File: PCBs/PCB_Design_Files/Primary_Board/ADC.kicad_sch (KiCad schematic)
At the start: 88 parts, among them U10 TMUX1133PWR, U11 MCP6561T-E/OT, U12 TMUX1133PWR, U13 LF398N/NOPB, U14 AD5621AKSZ, U15 TMUX1133PWR, U3 REF3333AIDBZR, U7 TMUX1104DGSR, U8 TMUX1133PWR, U9 TMUX1133PWR

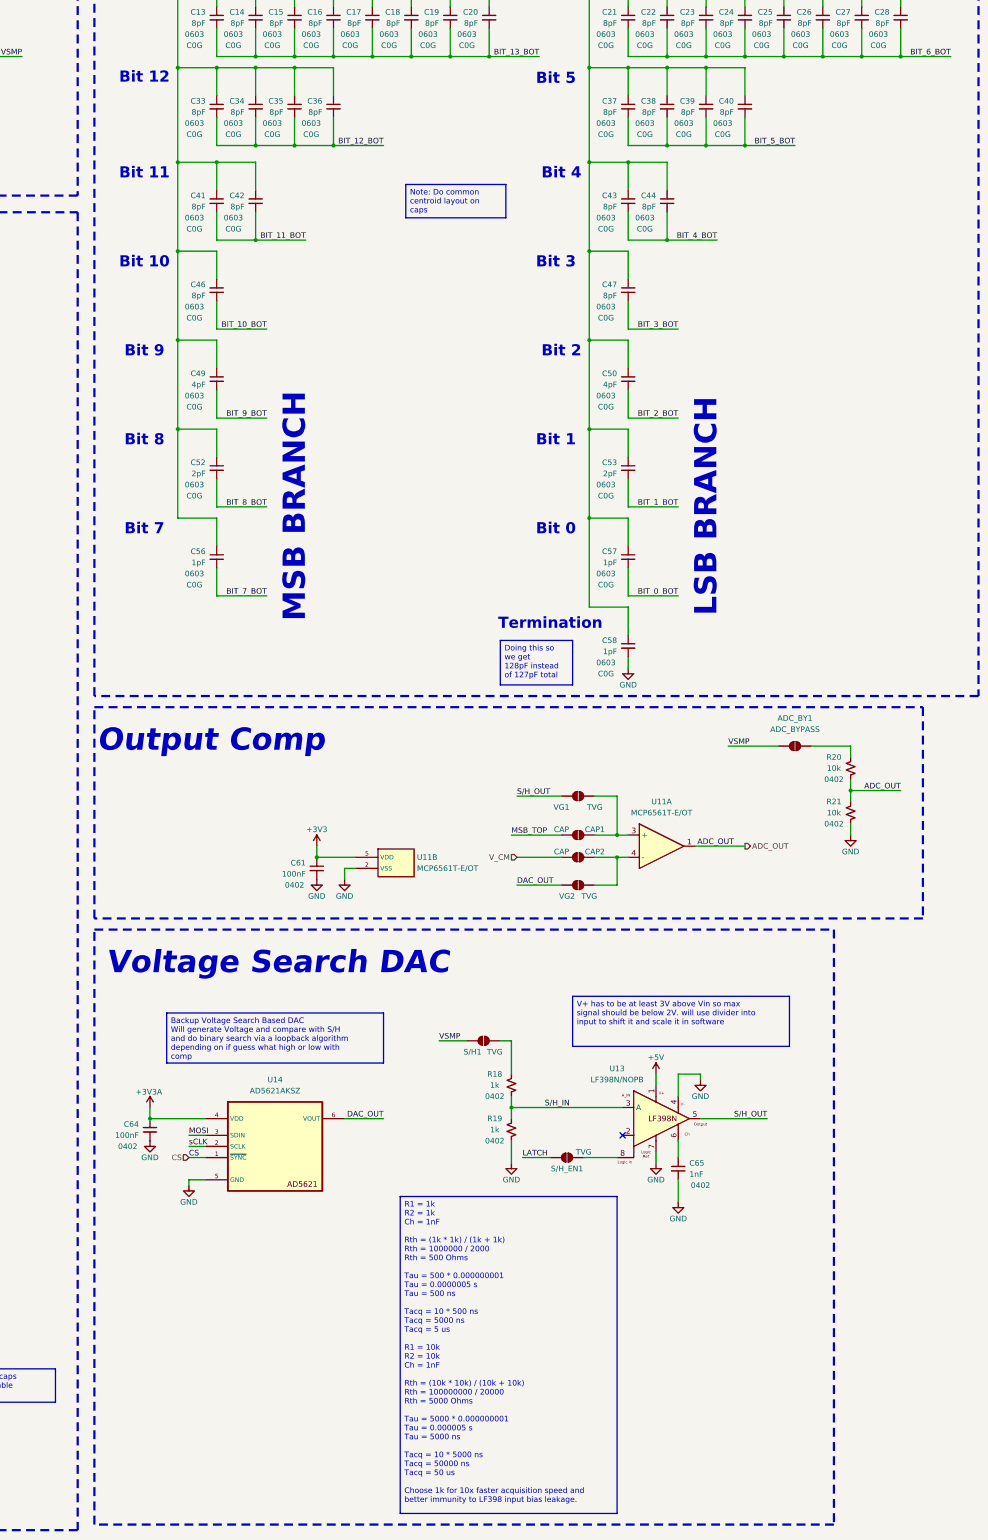
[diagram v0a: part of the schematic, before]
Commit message: Added Disctete S/H will simulate
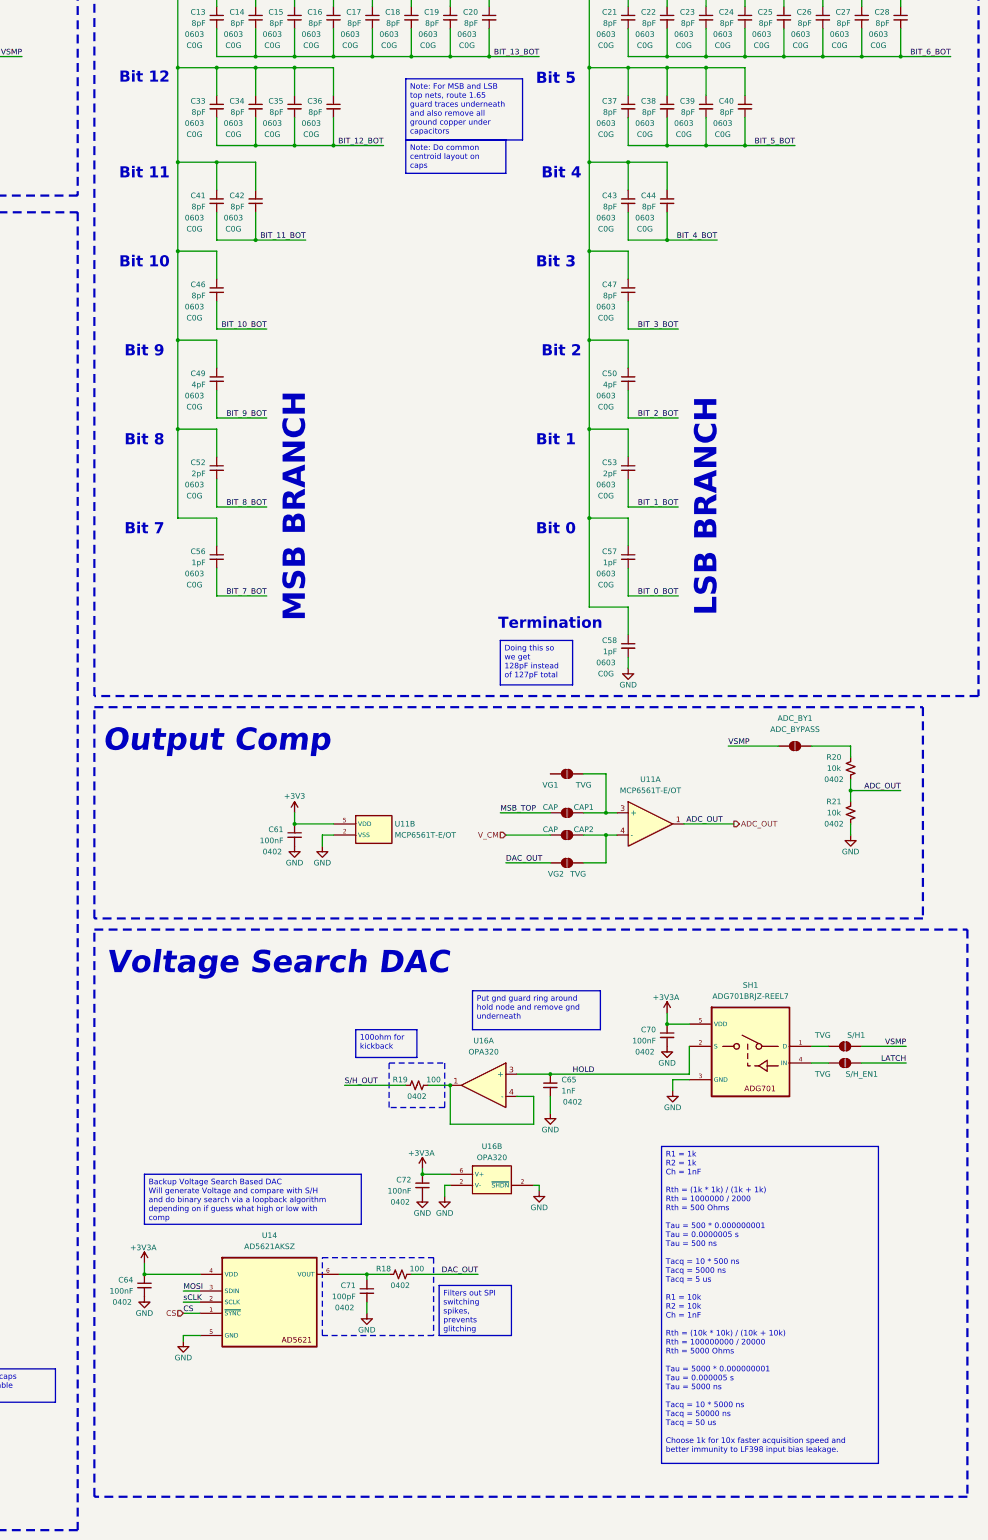
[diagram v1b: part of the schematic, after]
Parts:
- removed U13: LF398N/NOPB, Package_DIP:DIP-8_W7.62mm, symbol project_symbols:LF398N/NOPB
- added C70, C72: 100nF, Capacitor_SMD:C_0402_1005Metric, symbol Device:C_Small
- added C71: 100pF, Capacitor_SMD:C_0402_1005Metric, symbol Device:C_Small
- added SH1: ADG701BRJZ-REEL7, symbol project_symbols:ADG701BRJZ-REEL7
- added U16: OPA320, symbol project_symbols:OPA320
- R18, R19: value 1k -> 100
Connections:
- net +3V3A: now also C70.1, C72.1, SH1.5 (VDD), U16.6 (V+)
- net DAC_OUT: now also R18.2; no longer U14.6 (VOUT)
- net GND: now also C70.2, C71.2, C72.2, SH1.3 (GND), U16.2 (~{SHDN}); no longer R19.1
- net S/H_OUT: now also R19.1; no longer VG1.1 (A)
- net HOLD: now reaches C65.1
- net HOLD: now also SH1.2 (S), U16.3 (+)
- net at S/H1.2 (B): now also SH1.1 (D); no longer R18.2
- net at S/H_EN1.2 (B): now also SH1.4 (IN)
- net S/H_IN: no longer names the net of R18.1
- net S/H_IN: now also U14.6 (VOUT), C71.1; no longer R19.2
- new net: R19.2, U16.1, U16.4 (-)
- no-connect marks 4 -> 3
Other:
- moved on the sheet: C61, C64, C65, CAP1, CAP2, S/H1, S/H_EN1, U11A, U11B, U14, VG1, VG2

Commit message: Layed out all components, need to route
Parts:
- removed U16: OPA320, symbol project_symbols:OPA320
- added U13: OPA320SAIDBVR, Package_TO_SOT_SMD:SOT-23-6_Handsoldering, symbol project_symbols:OPA320
- SH1: footprint (none) -> Package_TO_SOT_SMD:SOT-23-5_HandSoldering
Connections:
- net +3V3A: now also U13.6 (V+)
- net GND: now also U13.2 (~{SHDN})
- net HOLD: now also U13.3 (+)
- net at R19.2: now also U13.1, U13.4 (-)
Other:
- moved on the sheet: C65

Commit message: schematic update
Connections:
- net S/H_OUT: now also VG1.1 (A)
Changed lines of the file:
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@@
+	(wire
+		(pts
+			(xy 364.49 218.44) (xy 374.65 218.44)
+		)
+		(stroke
+			(width 0)
+			(type default)
+		)
+	)
 	(wire
 		(pts
@@
 		)
 	)
+	(label "S{slash}H_OUT"
+		(at 364.49 218.44 0)
+		(effects
+			(font
+				(size 1.27 1.27)
+			)
+			(justify left bottom)
+		)
+	)

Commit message: Layout done, added more to bom for AFE, assigned all LCSC PNs and exported Gerbers for Top board, LOCATED IN /Users/oreoturkey/Documents/115DA-Capstone/PCBs/PCB_Design_Files/Primary_Board/jlcpcb/production files
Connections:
- net +3V3: now also U11.2 (VDD); no longer U11.5 (VDD)
- net GND: now also U11.5 (VSS); no longer U11.2 (VSS)
